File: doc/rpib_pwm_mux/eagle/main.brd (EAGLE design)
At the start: 49.2 x 45.7 mm, 21 parts, among them T1 2N2222, T10 2N2222, T11 2N2222, T7 2N2222, T8 2N2222, T9 2N2222

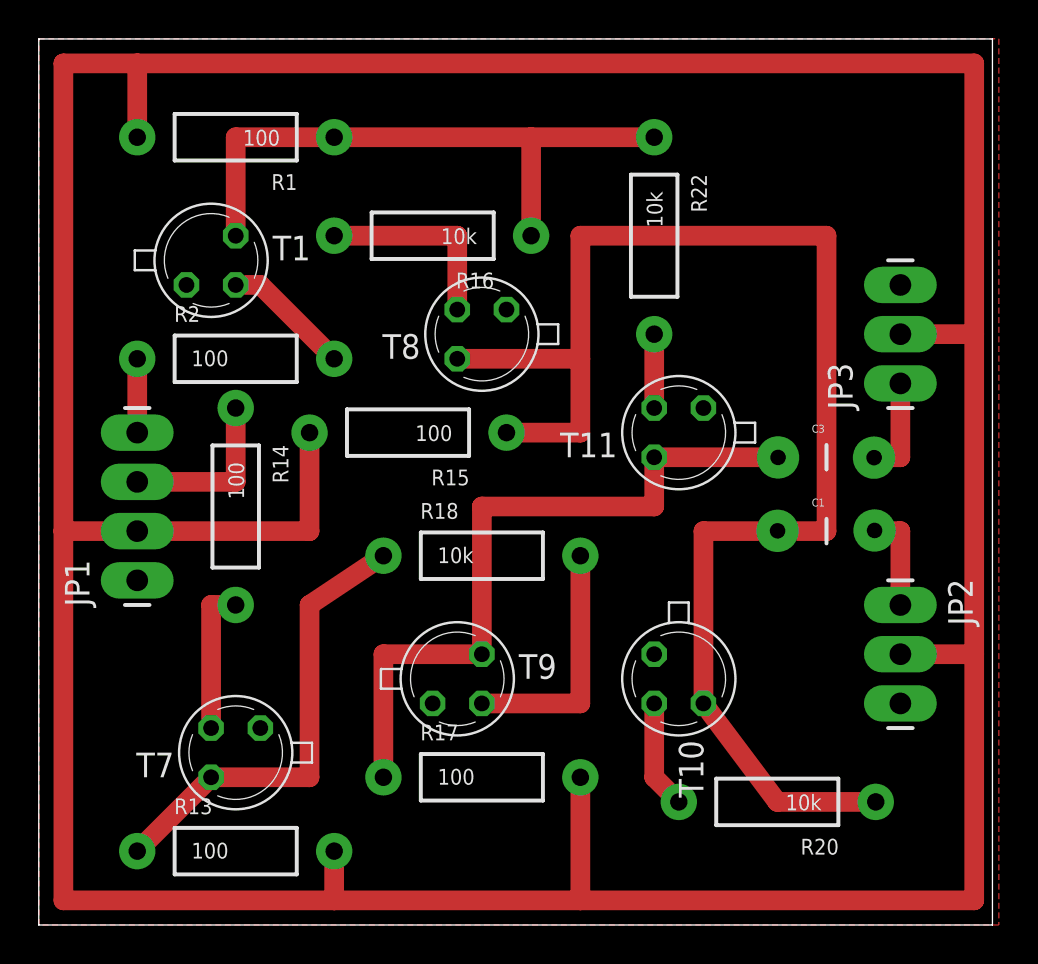
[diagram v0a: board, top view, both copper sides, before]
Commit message: [ fix ] rpib_pwm_mux eagle
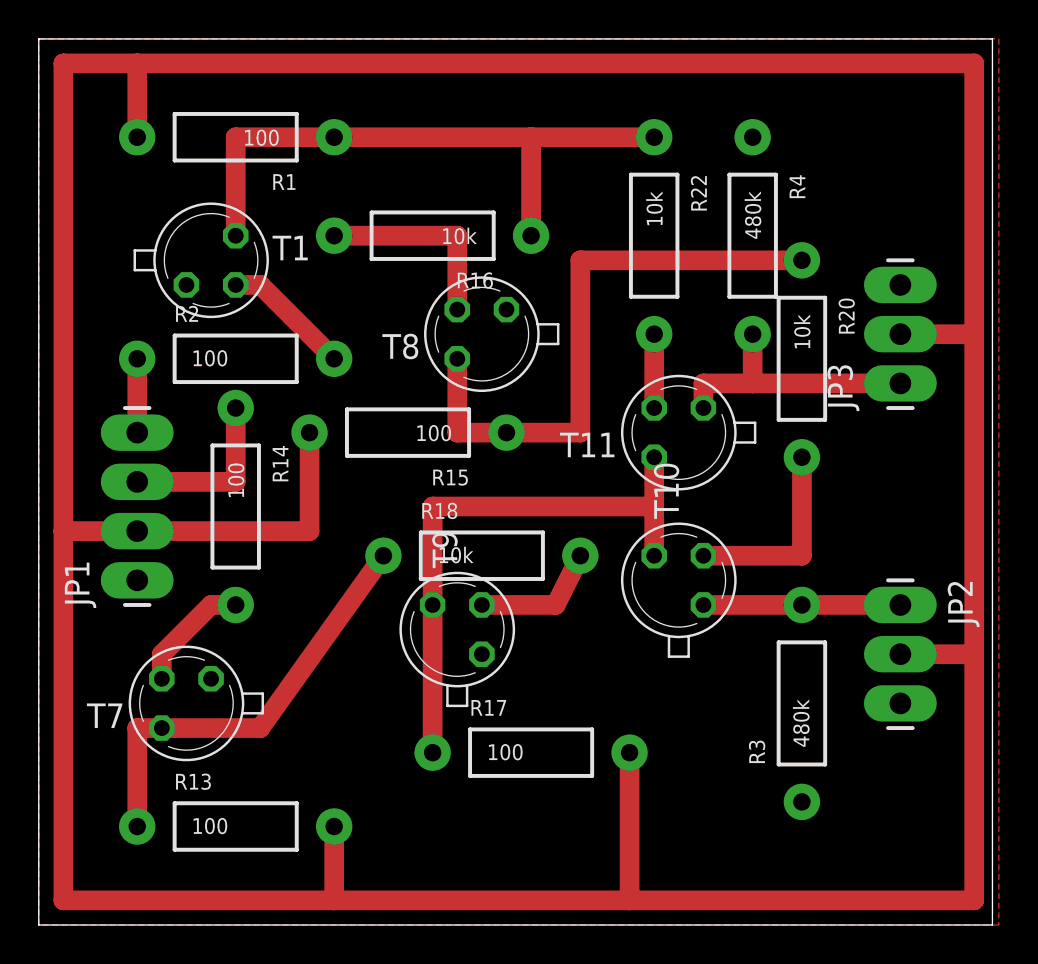
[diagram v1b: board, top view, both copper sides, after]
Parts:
- removed C1, C3: 100n, SparkFun:CAP-PTH-5MM
- added R3, R4: 480k, SparkFun:AXIAL-0.4
- moved R20 22.9 mm to (43.2, 41.9), turned to 270 degrees
- moved T10 5.08 mm to (36.8, 30.5), turned to 90 degrees
- moved T7 3.59 mm to (11.4, 24.1)
- moved R17 2.84 mm to (29.2, 21.6)
- moved T9 2.54 mm to (25.4, 27.9), turned to 90 degrees
- moved R13 1.27 mm to (14.0, 17.8)
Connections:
- net GND: now also R3.P$1, R4.P$1; no longer T10.1, T11.1
- net GPIO_5V: no longer C1.1, T10.3
- net PWM_5V: now also T10.3; no longer C3.1
- net SERVO_PWM_0: now also R3.P$2, T10.1; no longer C1.2
- net SERVO_PWM_1: now also R4.P$2, T11.1; no longer C3.2
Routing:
- net GPIO_5V: track 74.9 -> 30.5 mm
- net SERVO_PWM_1: track 5.12 -> 14.0 mm
- net PWM_5V: track 36.8 -> 29.2 mm
- net N$4: track 12.7 -> 6.65 mm
- net SERVO_PWM_0: track 5.12 -> 10.2 mm
- net N$5: track 5.61 -> 10.2 mm
- net 5V: track 218.4 -> 221.0 mm
- net PWM_BAR_5V: track 23.9 -> 22.4 mm
- net N$2: track 7.62 -> 6.13 mm

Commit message: [ update ] rpib_pwm_mux schematics, include capa to remove spikes
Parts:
- added C1, C2: 1n, SparkFun:CAP-PTH-SMALL-KIT
- moved R4 1.27 mm to (39.4, 48.3)
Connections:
- net GND: now also C1.2, C2.2
- net N$5: now also C1.1
- net N$6: now also C2.1
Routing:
- net N$6: track 3.81 -> 7.75 mm
- net N$5: track 10.2 -> 13.8 mm
- net GPIO_5V: track 30.5 -> 27.2 mm
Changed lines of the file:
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@@
 <layers>
 <layer number="1" name="Top" color="4" fill="1" visible="yes" active="yes"/>
-<layer number="16" name="Bottom" color="1" fill="1" visible="no" active="yes"/>
+<layer number="16" name="Bottom" color="1" fill="1" visible="yes" active="yes"/>
 <layer number="17" name="Pads" color="2" fill="1" visible="yes" active="yes"/>
 <layer number="18" name="Vias" color="2" fill="1" visible="yes" active="yes"/>
 <layer number="19" name="Unrouted" color="6" fill="1" visible="yes" active="yes"/>
-<layer number="20" name="Dimension" color="15" fill="1" visible="no" active="yes"/>
+<layer number="20" name="Dimension" color="15" fill="1" visible="yes" active="yes"/>
 <layer number="21" name="tPlace" color="7" fill="1" visible="yes" active="yes"/>
 <layer number="22" name="bPlace" color="7" fill="1" visible="no" active="yes"/>
 <layer number="23" name="tOrigins" color="15" fill="1" visible="yes" active="yes"/>
 <layer number="24" name="bOrigins" color="15" fill="1" visible="no" active="yes"/>
-<layer number="25" name="tNames" color="7" fill="1" visible="no" active="yes"/>
+<layer number="25" name="tNames" color="7" fill="1" visible="yes" active="yes"/>
 <layer number="26" name="bNames" color="7" fill="1" visible="no" active="yes"/>
 <layer number="27" name="tValues" color="7" fill="1" visible="no" active="yes"/>
@@
 <element name="JP3" library="SparkFun" package="1X03_LONGPADS" value="" x="48.26" y="40.64" rot="R90"/>
 <element name="R3" library="SparkFun" package="AXIAL-0.4" value="480k" x="43.18" y="24.13" rot="R90"/>
-<element name="R4" library="SparkFun" package="AXIAL-0.4" value="480k" x="40.64" y="48.26" rot="R270"/>
+<element name="R4" library="SparkFun" package="AXIAL-0.4" value="480k" x="39.37" y="48.26" rot="R270"/>
+<element name="C1" library="SparkFun" package="CAP-PTH-SMALL-KIT" value="1n" x="48.26" y="33.02"/>
+<element name="C2" library="SparkFun" package="CAP-PTH-SMALL-KIT" value="1n" x="31.75" y="38.1" rot="R270"/>
 </elements>
 <signals>
@@
 <contactref element="JP3" pad="2"/>
 <wire x1="48.26" y1="43.18" x2="52.07" y2="43.18" width="1.016" layer="1"/>
-<wire x1="52.07" y1="43.18" x2="52.07" y2="26.67" width="1.016" layer="1"/>
 <wire x1="48.26" y1="26.67" x2="52.07" y2="26.67" width="1.016" layer="1"/>
 <wire x1="52.07" y1="26.67" x2="52.07" y2="13.97" width="1.016" layer="1"/>
@@
 <wire x1="8.89" y1="33.02" x2="17.78" y2="33.02" width="1.016" layer="1"/>
 <wire x1="17.78" y1="33.02" x2="17.78" y2="38.1" width="1.016" layer="1"/>
+<wire x1="52.07" y1="43.18" x2="52.07" y2="26.67" width="1.016" layer="1"/>
 </signal>
 <signal name="GPIO_3V3">
@@
 <contactref element="JP2" pad="3"/>
 <contactref element="JP3" pad="3"/>
-<polygon width="0.4064" layer="1" isolate="0.8128">
+<polygon width="0.4064" layer="1" isolate="0.4064">
 <vertex x="3.81" y="58.42"/>
 <vertex x="53.34" y="58.42"/>
@@
 <contactref element="R3" pad="P$1"/>
 <contactref element="R4" pad="P$1"/>
+<contactref element="C1" pad="2"/>
+<contactref element="C2" pad="2"/>
 </signal>
 <signal name="GPIO_BAR_5V">
@@
 <wire x1="25.4" y1="41.91" x2="25.4" y2="38.1" width="1.016" layer="1"/>
 <wire x1="25.4" y1="38.1" x2="27.94" y2="38.1" width="1.016" layer="1"/>
-<wire x1="43.18" y1="46.99" x2="31.75" y2="46.99" width="1.016" layer="1"/>
-<wire x1="31.75" y1="46.99" x2="31.75" y2="38.1" width="1.016" layer="1"/>
-<wire x1="31.75" y1="38.1" x2="27.94" y2="38.1" width="1.016" layer="1"/>
+<wire x1="43.18" y1="46.99" x2="33.02" y2="46.99" width="1.016" layer="1"/>
+<wire x1="33.02" y1="46.99" x2="27.94" y2="40.64" width="1.016" layer="1"/>
+<wire x1="27.94" y1="40.64" x2="27.94" y2="38.1" width="1.016" layer="1"/>
 </signal>
 <signal name="PWM_5V">
@@
 <contactref element="R20" pad="P$2"/>
 <contactref element="T10" pad="2"/>
-<wire x1="38.1" y1="31.75" x2="43.18" y2="31.75" width="1.016" layer="1"/>
-<wire x1="43.18" y1="31.75" x2="43.18" y2="36.83" width="1.016" layer="1"/>
+<wire x1="38.1" y1="31.75" x2="38.1" y2="33.02" width="1.016" layer="1"/>
+<wire x1="38.1" y1="33.02" x2="43.18" y2="33.02" width="1.016" layer="1"/>
+<contactref element="C1" pad="1"/>
+<wire x1="43.18" y1="33.02" x2="43.18" y2="36.83" width="1.016" layer="1"/>
+<wire x1="46.863" y1="33.02" x2="43.18" y2="33.02" width="1.016" layer="1"/>
 </signal>
 <signal name="N$6">
@@
 <contactref element="T11" pad="2"/>
 <wire x1="35.56" y1="43.18" x2="35.56" y2="39.37" width="1.016" layer="1"/>
+<contactref element="C2" pad="1"/>
+<wire x1="31.75" y1="39.497" x2="35.56" y2="39.497" width="1.016" layer="1"/>
+<wire x1="35.56" y1="39.497" x2="35.56" y2="39.37" width="1.016" layer="1"/>
 </signal>
 <signal name="SERVO_PWM_0">
@@
 <contactref element="T11" pad="1"/>
 <contactref element="R4" pad="P$2"/>
-<wire x1="48.26" y1="40.64" x2="40.64" y2="40.64" width="1.016" layer="1"/>
-<wire x1="40.64" y1="40.64" x2="38.1" y2="40.64" width="1.016" layer="1"/>
+<wire x1="48.26" y1="40.64" x2="39.37" y2="40.64" width="1.016" layer="1"/>
+<wire x1="39.37" y1="40.64" x2="38.1" y2="40.64" width="1.016" layer="1"/>
 <wire x1="38.1" y1="40.64" x2="38.1" y2="39.37" width="1.016" layer="1"/>
-<wire x1="40.64" y1="43.18" x2="40.64" y2="40.64" width="1.016" layer="1"/>
+<wire x1="39.37" y1="43.18" x2="39.37" y2="40.64" width="1.016" layer="1"/>
 </signal>
 </signals>
